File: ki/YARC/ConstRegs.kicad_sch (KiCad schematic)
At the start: 10 parts, among them U65 74LS32, U91 74HC245, U92 74LS157, U93 74LS32, U94 74HC245, U95 74HC245, U96 74LS32, U97 74HC00, U98 74HC245, U99 74HC245

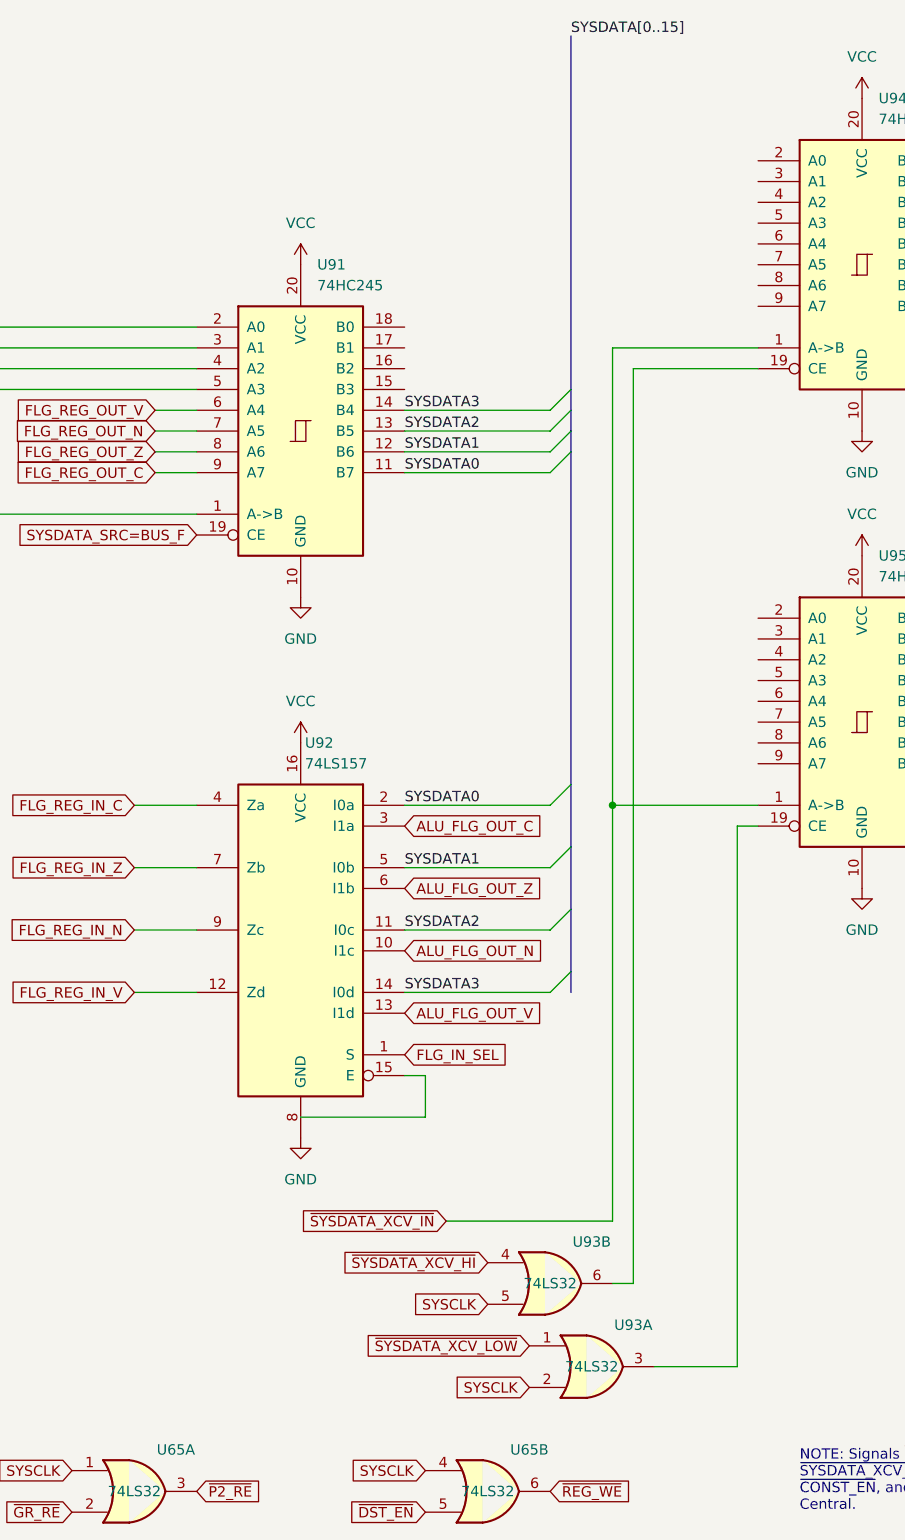
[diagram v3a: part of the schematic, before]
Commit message: Add register enable to MCR. Corrections and cleanups.
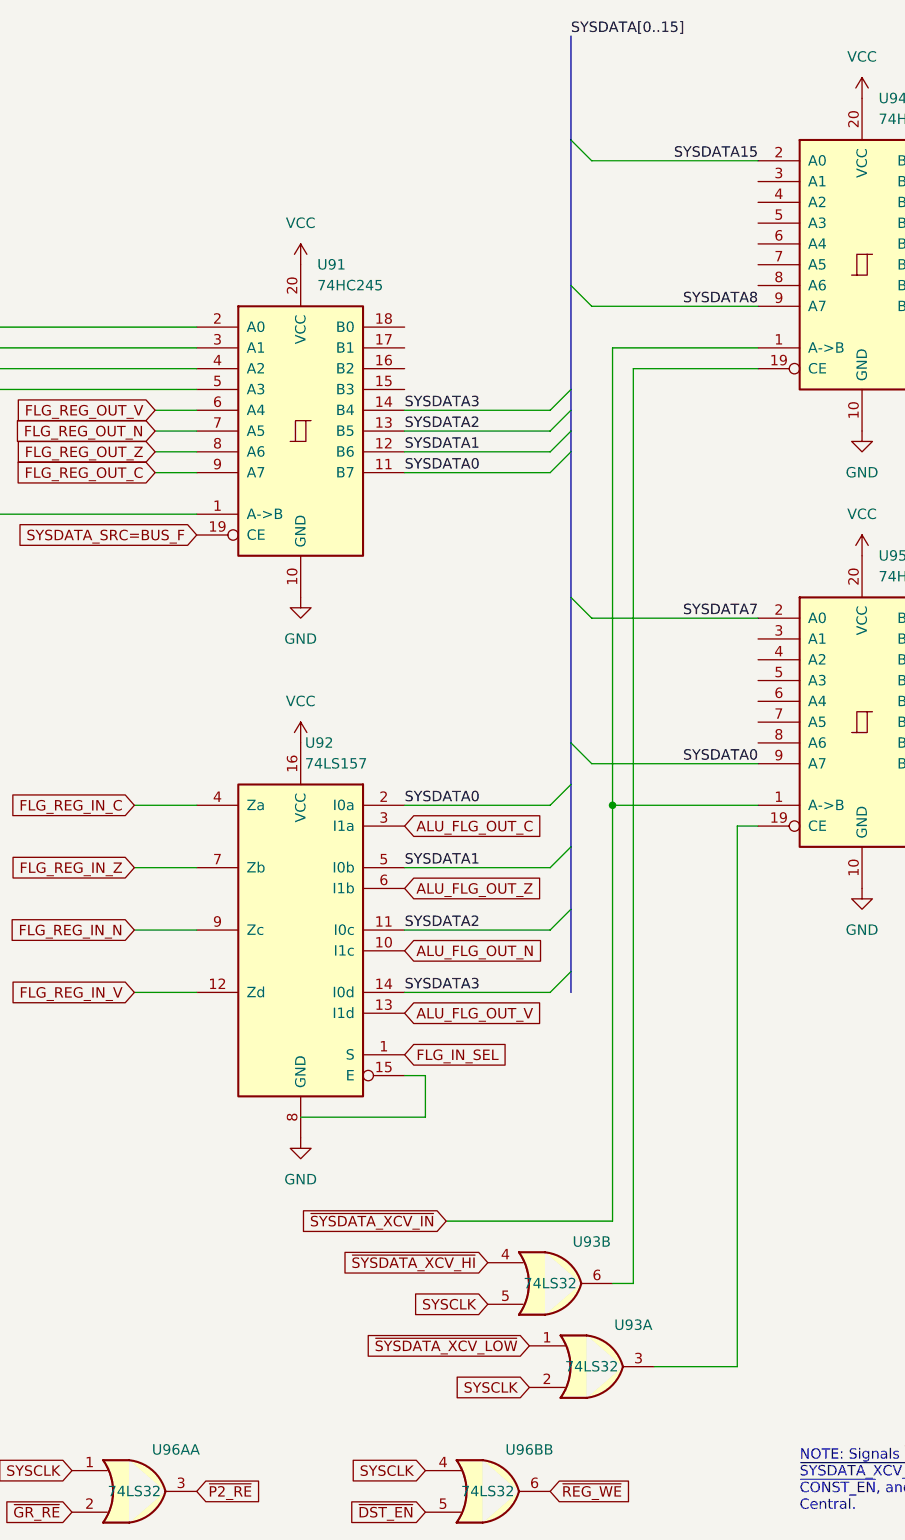
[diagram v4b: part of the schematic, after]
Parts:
- renumbered U65 to U96A, U65 to U96B
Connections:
- net SYSDATA0: now also U95.9 (A7)
- net SYSDATA15: now reaches U94.2 (A0)
- net SYSDATA8: now reaches U94.9 (A7)
- net SYSDATA7: now reaches U95.2 (A0)
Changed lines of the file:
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@@
+    (stroke (width 0) (type default) (color 0 0 0 0))
+  )
+  (bus_entry (at 88.9 86.36) (size 2.54 2.54)
     (stroke (width 0) (type default) (color 0 0 0 0))
   )
@@
     (stroke (width 0) (type default) (color 0 0 0 0))
   )
+  (bus_entry (at 88.9 104.14) (size 2.54 2.54)
+    (stroke (width 0) (type default) (color 0 0 0 0))
+  )
   (bus_entry (at 154.94 48.26) (size 2.54 2.54)
     (stroke (width 0) (type default) (color 0 0 0 0))
   )
+  (bus_entry (at 88.9 48.26) (size 2.54 2.54)
+    (stroke (width 0) (type default) (color 0 0 0 0))
+  )
   (bus_entry (at 88.9 124.46) (size -2.54 2.54)
     (stroke (width 0) (type default) (color 0 0 0 0))
@@
     (stroke (width 0) (type default) (color 0 0 0 0))
   )
+  (bus_entry (at 88.9 30.48) (size 2.54 2.54)
+    (stroke (width 0) (type default) (color 0 0 0 0))
+  )
   (bus_entry (at 88.9 63.5) (size -2.54 2.54)
     (stroke (width 0) (type default) (color 0 0 0 0))
@@
     (stroke (width 0) (type default) (color 0 0 0 0))
   )
+  (wire (pts (xy 91.44 88.9) (xy 111.76 88.9))
+    (stroke (width 0) (type default) (color 0 0 0 0))
+  )
   (wire (pts (xy 134.62 172.72) (xy 134.62 167.64))
     (stroke (width 0) (type default) (color 0 0 0 0))
@@
     (stroke (width 0) (type default) (color 0 0 0 0))
   )
+  (wire (pts (xy 91.44 106.68) (xy 111.76 106.68))
+    (stroke (width 0) (type default) (color 0 0 0 0))
+  )
   (wire (pts (xy 96.52 170.18) (xy 96.52 58.42))
     (stroke (width 0) (type default) (color 0 0 0 0))
@@
     (stroke (width 0) (type default) (color 0 0 0 0))
   )
-  (bus (pts (xy 88.9 17.78) (xy 88.9 60.96))
+  (bus (pts (xy 88.9 17.78) (xy 88.9 30.48))
     (stroke (width 0) (type default) (color 0 0 0 0))
   )
@@
     (stroke (width 0) (type default) (color 0 0 0 0))
   )
+  (bus (pts (xy 88.9 30.48) (xy 88.9 48.26))
+    (stroke (width 0) (type default) (color 0 0 0 0))
+  )
   (wire (pts (xy 190.5 119.38) (xy 193.04 119.38))
     (stroke (width 0) (type default) (color 0 0 0 0))
@@
     (stroke (width 0) (type default) (color 0 0 0 0))
   )
-  (bus (pts (xy 88.9 68.58) (xy 88.9 109.22))
+  (bus (pts (xy 88.9 68.58) (xy 88.9 86.36))
     (stroke (width 0) (type default) (color 0 0 0 0))
   )
@@
     (stroke (width 0) (type default) (color 0 0 0 0))
   )
+  (wire (pts (xy 91.44 33.02) (xy 111.76 33.02))
+    (stroke (width 0) (type default) (color 0 0 0 0))
+  )
   (wire (pts (xy 220.98 45.72) (xy 220.98 48.26))
     (stroke (width 0) (type default) (color 0 0 0 0))
@@
     (stroke (width 0) (type default) (color 0 0 0 0))
   )
+  (bus (pts (xy 88.9 86.36) (xy 88.9 104.14))
+    (stroke (width 0) (type default) (color 0 0 0 0))
+  )
   (bus (pts (xy 88.9 63.5) (xy 88.9 66.04))
     (stroke (width 0) (type default) (color 0 0 0 0))
@@
     (stroke (width 0) (type default) (color 0 0 0 0))
   )
+  (bus (pts (xy 88.9 48.26) (xy 88.9 60.96))
+    (stroke (width 0) (type default) (color 0 0 0 0))
+  )
   (wire (pts (xy 208.28 66.04) (xy 208.28 71.12))
     (stroke (width 0) (type default) (color 0 0 0 0))
@@
     (stroke (width 0) (type default) (color 0 0 0 0))
   )
+  (wire (pts (xy 91.44 50.8) (xy 111.76 50.8))
+    (stroke (width 0) (type default) (color 0 0 0 0))
+  )
   (wire (pts (xy 93.98 55.88) (xy 111.76 55.88))
+    (stroke (width 0) (type default) (color 0 0 0 0))
+  )
+  (bus (pts (xy 88.9 104.14) (xy 88.9 109.22))
     (stroke (width 0) (type default) (color 0 0 0 0))
   )
@@
     (effects (font (size 1.27 1.27)) (justify left bottom))
   )
+  (label "SYSDATA0" (at 111.76 106.68 180)
+    (effects (font (size 1.27 1.27)) (justify right bottom))
+  )
   (label "S2BUS7" (at 137.16 88.9 0)
     (effects (font (size 1.27 1.27)) (justify left bottom))
@@
     (effects (font (size 1.27 1.27)) (justify left bottom))
   )
+  (label "SYSDATA8" (at 111.76 50.8 180)
+    (effects (font (size 1.27 1.27)) (justify right bottom))
+  )
+  (label "SYSDATA7" (at 111.76 88.9 180)
+    (effects (font (size 1.27 1.27)) (justify right bottom))
+  )
   (label "SYSDATA1" (at 68.58 68.58 0)
     (effects (font (size 1.27 1.27)) (justify left bottom))
@@
   (label "SYSDATA[0..15]" (at 88.9 17.78 0)
     (effects (font (size 1.27 1.27)) (justify left bottom))
+  )
+  (label "SYSDATA15" (at 111.76 33.02 180)
+    (effects (font (size 1.27 1.27)) (justify right bottom))
   )
   (label "SYSDATA3" (at 68.58 134.62 0)
@@
   (symbol (lib_id "74xx:74LS32") (at 35.56 195.58 0) (unit 1)
     (in_bom yes) (on_board yes)
-    (property "Reference" "U65" (id 0) (at 40.64 190.5 0))
+    (property "Reference" "U96A" (id 0) (at 40.64 190.5 0))
     (property "Value" "74LS32" (id 1) (at 35.56 195.58 0))
     (property "Footprint" "" (id 2) (at 35.56 195.58 0)
@@
   (symbol (lib_id "74xx:74LS32") (at 78.74 195.58 0) (unit 2)
     (in_bom yes) (on_board yes)
-    (property "Reference" "U65" (id 0) (at 83.82 190.5 0))
+    (property "Reference" "U96B" (id 0) (at 83.82 190.5 0))
     (property "Value" "74LS32" (id 1) (at 78.74 195.58 0))
     (property "Footprint" "" (id 2) (at 78.74 195.58 0)

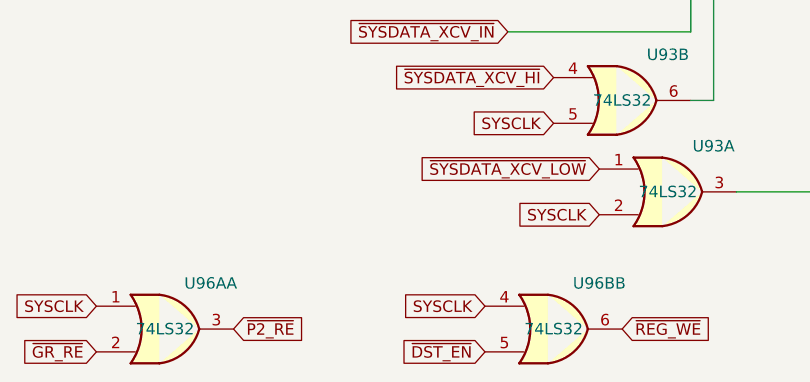
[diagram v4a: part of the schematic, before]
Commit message: Major changes to ALU, Flags, and add new ALU controls schematic
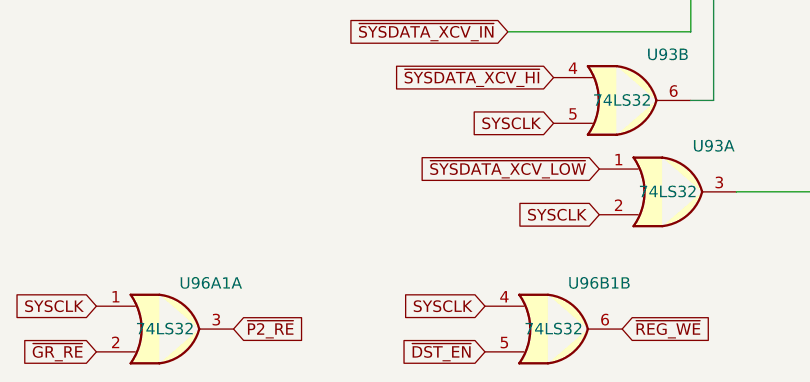
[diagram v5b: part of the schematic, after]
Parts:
- renumbered U96A to U96A1, U96B to U96B1
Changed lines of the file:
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@@
   (symbol (lib_id "74xx:74LS32") (at 35.56 195.58 0) (unit 1)
     (in_bom yes) (on_board yes)
-    (property "Reference" "U96A" (id 0) (at 40.64 190.5 0))
+    (property "Reference" "U96A1" (id 0) (at 40.64 190.5 0))
     (property "Value" "74LS32" (id 1) (at 35.56 195.58 0))
     (property "Footprint" "" (id 2) (at 35.56 195.58 0)
@@
   (symbol (lib_id "74xx:74LS32") (at 78.74 195.58 0) (unit 2)
     (in_bom yes) (on_board yes)
-    (property "Reference" "U96B" (id 0) (at 83.82 190.5 0))
+    (property "Reference" "U96B1" (id 0) (at 83.82 190.5 0))
     (property "Value" "74LS32" (id 1) (at 78.74 195.58 0))
     (property "Footprint" "" (id 2) (at 78.74 195.58 0)

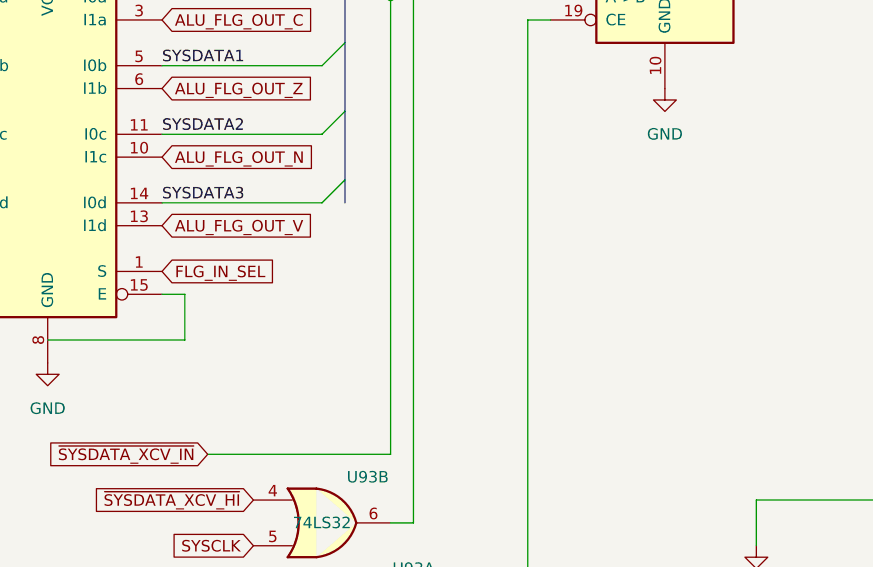
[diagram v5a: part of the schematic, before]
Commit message: Ongoing development of ALU and Flags. Construction start.
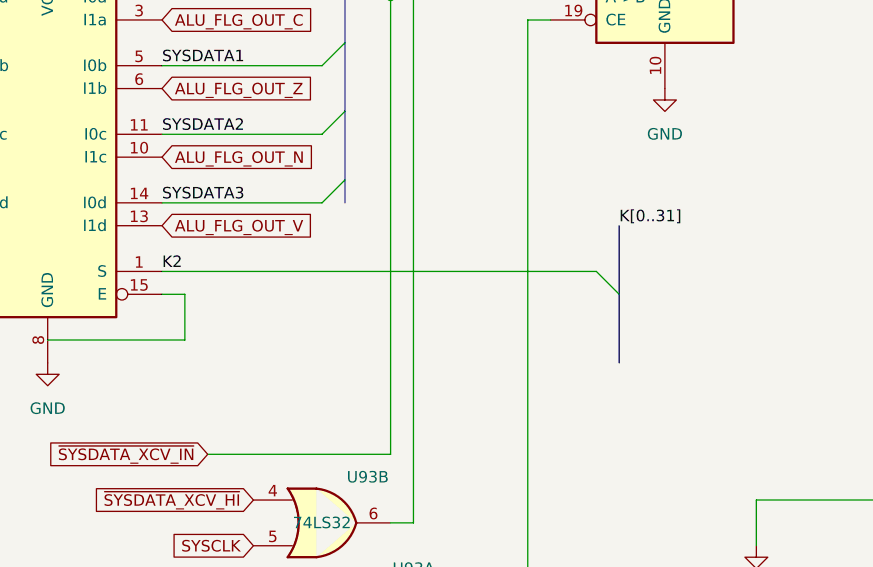
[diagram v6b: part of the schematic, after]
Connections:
- net FLG_IN_SEL renamed K2
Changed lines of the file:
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@@
+    (stroke (width 0) (type default) (color 0 0 0 0))
+  )
+  (bus_entry (at 119.38 144.78) (size -2.54 -2.54)
     (stroke (width 0) (type default) (color 0 0 0 0))
   )
@@
     (stroke (width 0) (type default) (color 0 0 0 0))
   )
+  (bus (pts (xy 119.38 144.78) (xy 119.38 152.4))
+    (stroke (width 0) (type default) (color 0 0 0 0))
+  )
   (wire (pts (xy 91.44 106.68) (xy 111.76 106.68))
     (stroke (width 0) (type default) (color 0 0 0 0))
@@
     (stroke (width 0) (type default) (color 0 0 0 0))
   )
+  (wire (pts (xy 116.84 142.24) (xy 68.58 142.24))
+    (stroke (width 0) (type default) (color 0 0 0 0))
+  )
   (bus (pts (xy 88.9 109.22) (xy 88.9 116.84))
     (stroke (width 0) (type default) (color 0 0 0 0))
@@
   )
   (wire (pts (xy 134.62 167.64) (xy 154.94 167.64))
+    (stroke (width 0) (type default) (color 0 0 0 0))
+  )
+  (bus (pts (xy 119.38 137.16) (xy 119.38 144.78))
     (stroke (width 0) (type default) (color 0 0 0 0))
   )
@@
     (effects (font (size 1.27 1.27)) (justify left bottom))
   )
+  (label "K2" (at 68.58 142.24 0)
+    (effects (font (size 1.27 1.27)) (justify left bottom))
+  )
   (label "SYSDATA3" (at 68.58 63.5 0)
     (effects (font (size 1.27 1.27)) (justify left bottom))
@@
   (label "SYSDATA8" (at 111.76 50.8 180)
     (effects (font (size 1.27 1.27)) (justify right bottom))
+  )
+  (label "K[0..31]" (at 119.38 137.16 0)
+    (effects (font (size 1.27 1.27)) (justify left bottom))
   )
   (label "SYSDATA7" (at 111.76 88.9 180)
@@
     )
   )
-  (global_label "FLG_IN_SEL" (shape input) (at 68.58 142.24 0) (fields_autoplaced)
-    (effects (font (size 1.27 1.27)) (justify left))
-    (property "Intersheet References" "${INTERSHEET_REFS}" (id 0) (at 81.6369 142.1606 0)
-      (effects (font (size 1.27 1.27)) (justify left) hide)
-    )
-  )

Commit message: Various corrections and minor improvements
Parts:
- removed U91: 74HC245, symbol 74xx:74HC245
- removed U92: 74LS157, symbol 74xx:74LS157
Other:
- moved on the sheet: U93A, U93B, U96A1A, U96B1B

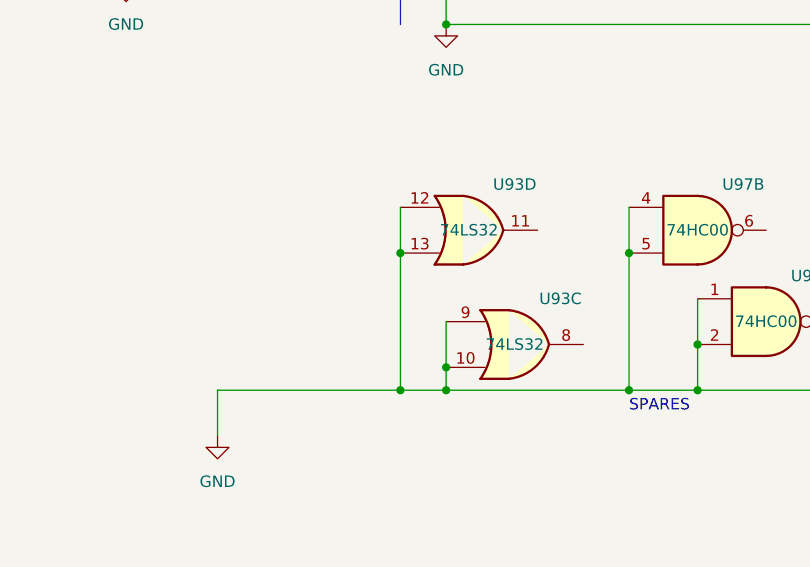
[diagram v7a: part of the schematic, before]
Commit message: Updates for ad hoc wiring changes
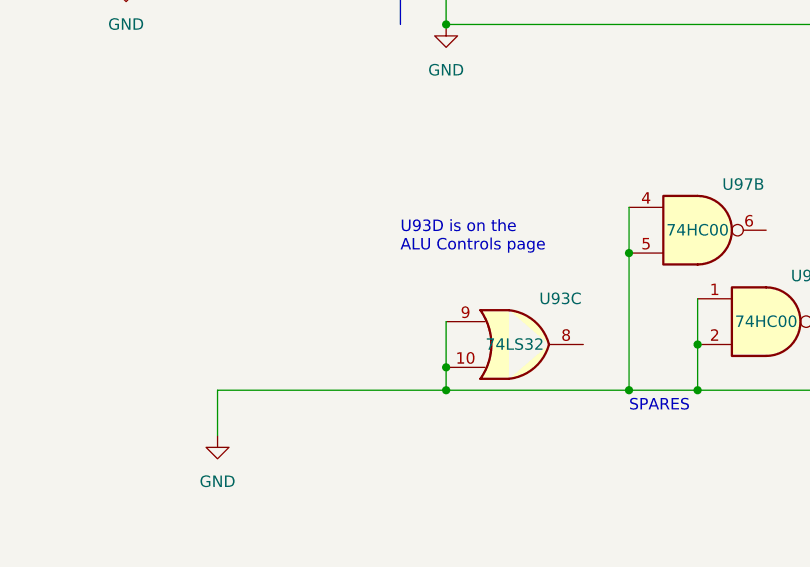
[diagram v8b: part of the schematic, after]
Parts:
- removed unit 4 of U93
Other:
- note added: "U93D is on the ALU Controls page"
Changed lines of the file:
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@@
   (junction (at 251.46 83.82) (diameter 0) (color 0 0 0 0)
   )
-  (junction (at 154.94 152.4) (diameter 0) (color 0 0 0 0)
-  )
   (junction (at 187.96 162.56) (diameter 0) (color 0 0 0 0)
   )
@@
   (junction (at 220.98 101.6) (diameter 0) (color 0 0 0 0)
   )
-  (junction (at 154.94 167.64) (diameter 0) (color 0 0 0 0)
-  )
   (junction (at 251.46 86.36) (diameter 0) (color 0 0 0 0)
   )
@@
     (stroke (width 0) (type default) (color 0 0 0 0))
   )
-  (wire (pts (xy 154.94 152.4) (xy 154.94 167.64))
-    (stroke (width 0) (type default) (color 0 0 0 0))
-  )
   (wire (pts (xy 264.16 139.7) (xy 264.16 63.5))
     (stroke (width 0) (type default) (color 0 0 0 0))
@@
     (stroke (width 0) (type default) (color 0 0 0 0))
   )
-  (wire (pts (xy 154.94 167.64) (xy 160.02 167.64))
+  (wire (pts (xy 134.62 167.64) (xy 160.02 167.64))
     (stroke (width 0) (type default) (color 0 0 0 0))
   )
@@
     (stroke (width 0) (type default) (color 0 0 0 0))
   )
-  (wire (pts (xy 134.62 167.64) (xy 154.94 167.64))
-    (stroke (width 0) (type default) (color 0 0 0 0))
-  )
   (wire (pts (xy 246.38 76.2) (xy 251.46 76.2))
     (stroke (width 0) (type default) (color 0 0 0 0))
@@
   )
   (wire (pts (xy 220.98 106.68) (xy 223.52 106.68))
-    (stroke (width 0) (type default) (color 0 0 0 0))
-  )
-  (wire (pts (xy 154.94 147.32) (xy 154.94 152.4))
     (stroke (width 0) (type default) (color 0 0 0 0))
   )
@@
   )
   (text "SPARES" (at 180.34 170.18 0)
+    (effects (font (size 1.27 1.27)) (justify left bottom))
+  )
+  (text "U93D is on the\nALU Controls page" (at 154.94 152.4 0)
     (effects (font (size 1.27 1.27)) (justify left bottom))
   )
@@
     (pin "1")
   )
-  (symbol (lib_id "74xx:74LS32") (at 162.56 149.86 0) (unit 4)
-    (in_bom yes) (on_board yes)
-    (property "Reference" "U93" (id 0) (at 167.64 144.78 0))
-    (property "Value" "74LS32" (id 1) (at 162.56 149.86 0))
-    (property "Footprint" "" (id 2) (at 162.56 149.86 0)
-      (effects (font (size 1.27 1.27)) hide)
-    )
-    (property "Datasheet" "http://www.ti.com/lit/gpn/sn74LS32" (id 3) (at 162.56 149.86 0)
-      (effects (font (size 1.27 1.27)) hide)
-    )
-    (pin "11")
-    (pin "12")
-    (pin "13")
-  )
   (symbol (lib_id "power:VCC") (at 124.46 81.28 0) (unit 1)
